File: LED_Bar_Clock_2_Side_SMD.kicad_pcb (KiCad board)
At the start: 2 copper layers, 100 x 100 mm, 52 parts, among them J1 U262-16XN-4BVC11, J2 AVR-ISP-6, SW1 SKHMQKE010, SW2 SW_5_Way, U1 ATtiny84A-SSUR, U2 DS1307Z+, Y1 32.768 kHz

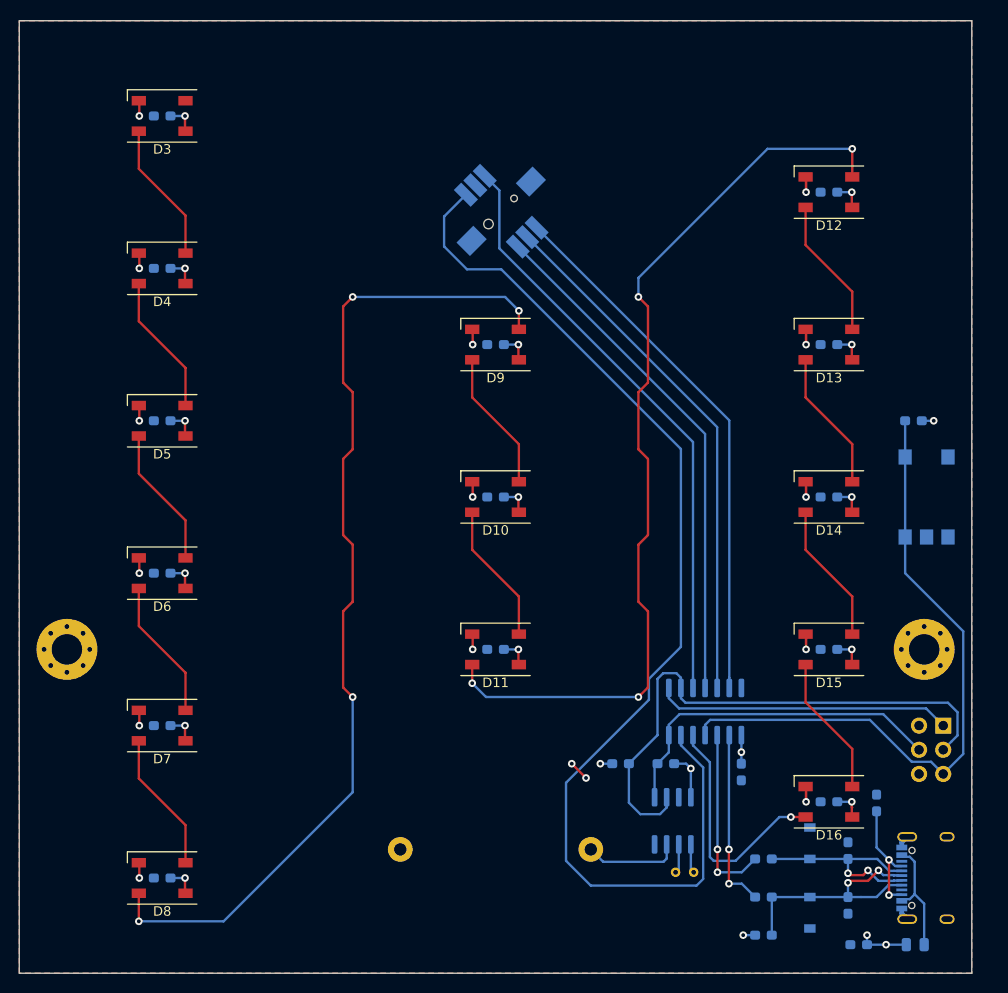
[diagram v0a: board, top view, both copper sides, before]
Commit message: silkscreen and stealth labels
add a stealth footprint for the leds because we dont need silkscreen
on the front

official name is FILO Clock
first illuminated last out
.. or ..
first ignited last out
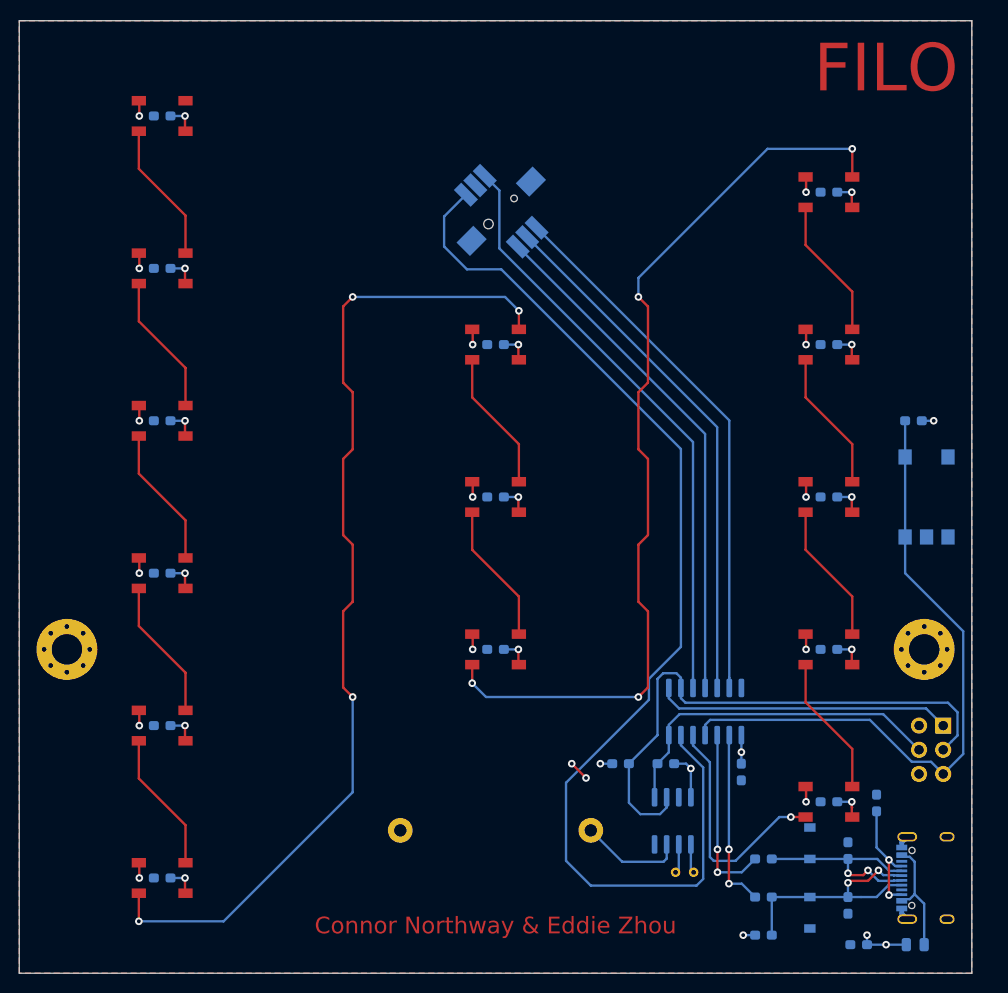
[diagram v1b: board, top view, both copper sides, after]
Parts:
- D10, D11, D12, D13, D14, D15, D16, D3, D4, D5, D6, D7, D8, D9: footprint LED_SMD:LED_SK6812_PLCC4_5.0x5.0mm_P3.2mm -> Clock_Footprints:LED_SK6812_PLCC4_5.0x5.0mm_P3.2mm_STEALTH
- moved BT1 2.00 mm to (97.8, 135.0)
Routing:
- net Net-(BT1-Pad1): track 10.1 -> 11.0 mm
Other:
- board text added: "Connor Northway & Eddie Zhou"
- board text added: "FILO"
- board text added: "FILO Clock v1.0"
